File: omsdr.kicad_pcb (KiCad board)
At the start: 2 copper layers, 50 x 50 mm, 58 parts, among them J1 I/Q Out, J2 ANT, J3 ISP, J4 LO, J5 I/Q Out, J8 PWR, SW1 SW_SPST, SW2 SW_SPST, T1 CX2074NL, U1 LT6231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

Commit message: Adding year 2022 to copyright info
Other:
- board text added: "Based on work by T. Parks (c) 2017,18,19,22 CC-BY-SA"
- board text removed: "Based on work by T. Parks (c) 2017,18,19 CC-BY-SA"
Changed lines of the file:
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@@
   (gr_line (start 147.5 100) (end 102.5 100) (layer "Edge.Cuts") (width 0.15))
   (gr_arc (start 102.5 100) (mid 100.732233 99.267767) (end 100 97.5) (layer "Edge.Cuts") (width 0.15))
-  (gr_text "Based on work by T. Parks\n(c) 2017,18,19 CC-BY-SA" (at 148 89.25) (layer "B.SilkS")
+  (gr_text "Based on work by T. Parks\n(c) 2017,18,19,22 CC-BY-SA" (at 148 89.25) (layer "B.SilkS")
     (effects (font (size 0.75 0.75) (thickness 0.15)) (justify left mirror))
   )

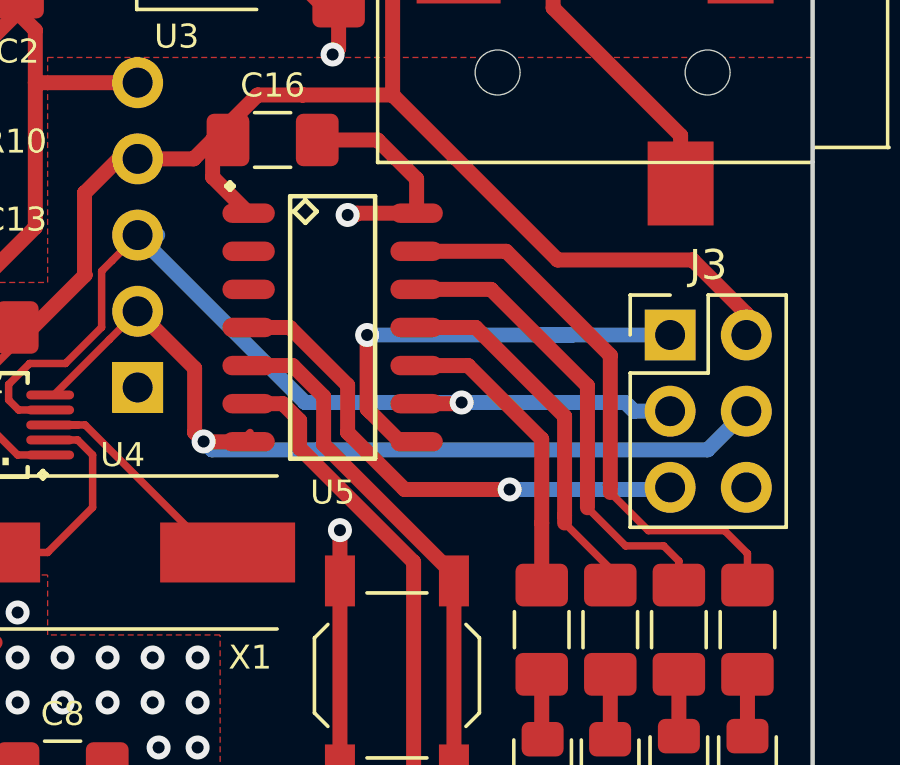
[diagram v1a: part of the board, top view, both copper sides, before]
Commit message: Using attiny24 from the KiCad library (sch & pcb)
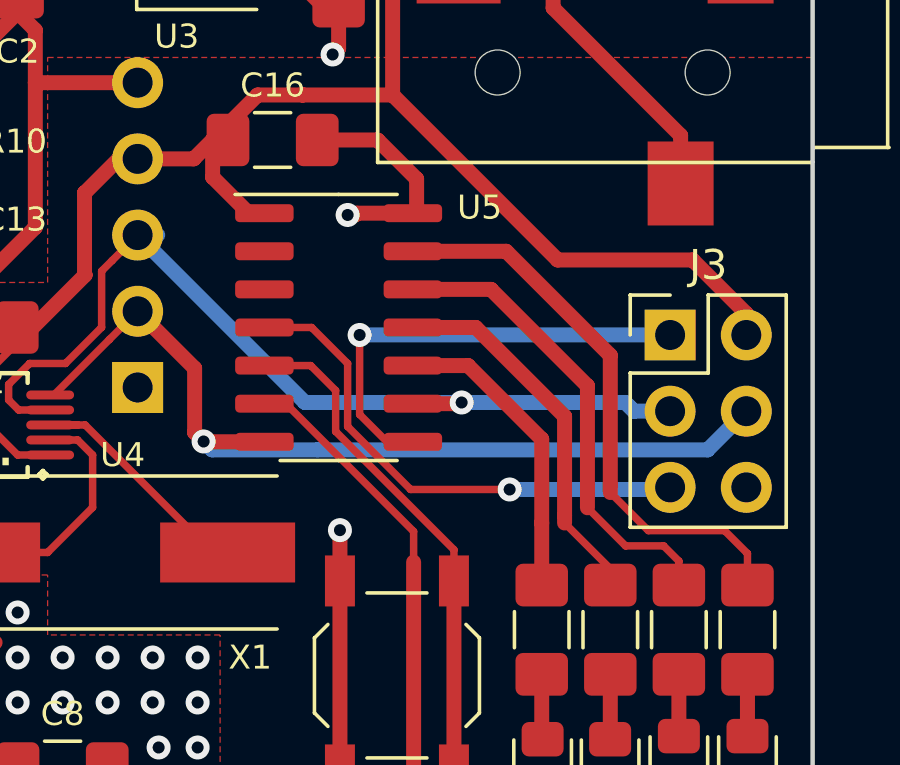
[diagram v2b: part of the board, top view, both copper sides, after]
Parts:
- U5: value ATTINY24-20SSU -> ATtiny24-20SS; footprint IPC7351-Most:SOIC127P600X175-14 -> Package_SO:SOIC-14_3.9x8.7mm_P1.27mm
- moved U5 0.20 mm to (134.2, 74.0)
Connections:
- net /MOSI renamed /SDA
- net /SCK renamed /SCL
- U2 pad 10: Net-(U2-Pad10) -> unconnected-(U2-Pad10)
- U2 pad 13: Net-(U2-Pad13) -> unconnected-(U2-Pad13)
- U2 pad 4: Net-(U2-Pad4) -> unconnected-(U2-Pad4)
- U2 pad 5: Net-(U2-Pad5) -> unconnected-(U2-Pad5)
- U4 pad 6: Net-(U4-Pad6) -> unconnected-(U4-Pad6)
- U5 pad 2: Net-(U5-Pad2) -> unconnected-(U5-Pad2)
- U5 pad 3: Net-(U5-Pad3) -> unconnected-(U5-Pad3)
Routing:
- net /SDA: track 30.3 -> 29.6 mm
- net /BUTTON2: track 24.9 -> 25.6 mm

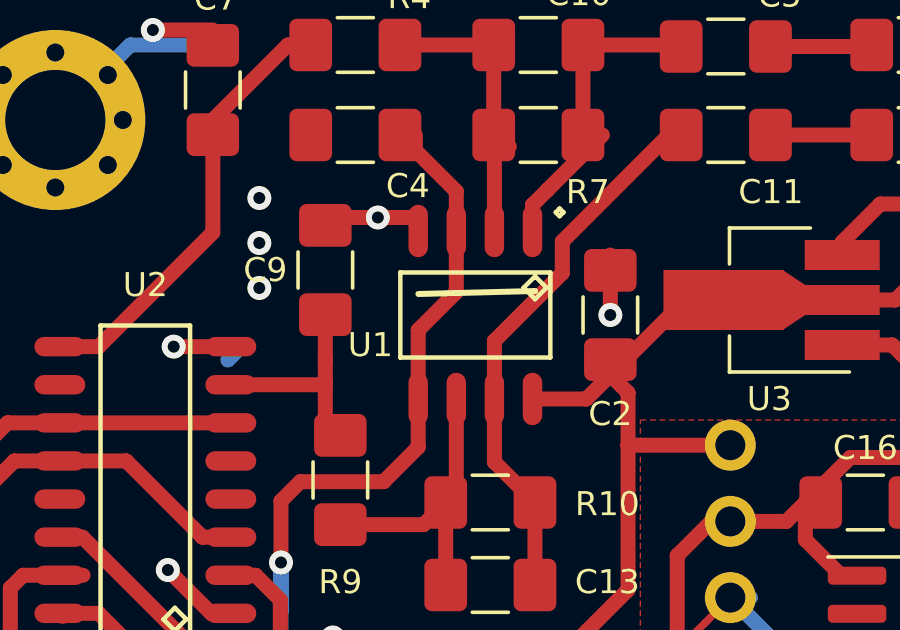
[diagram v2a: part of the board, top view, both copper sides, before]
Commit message: Using LC6231 from the KiCad library (sch & pcb)
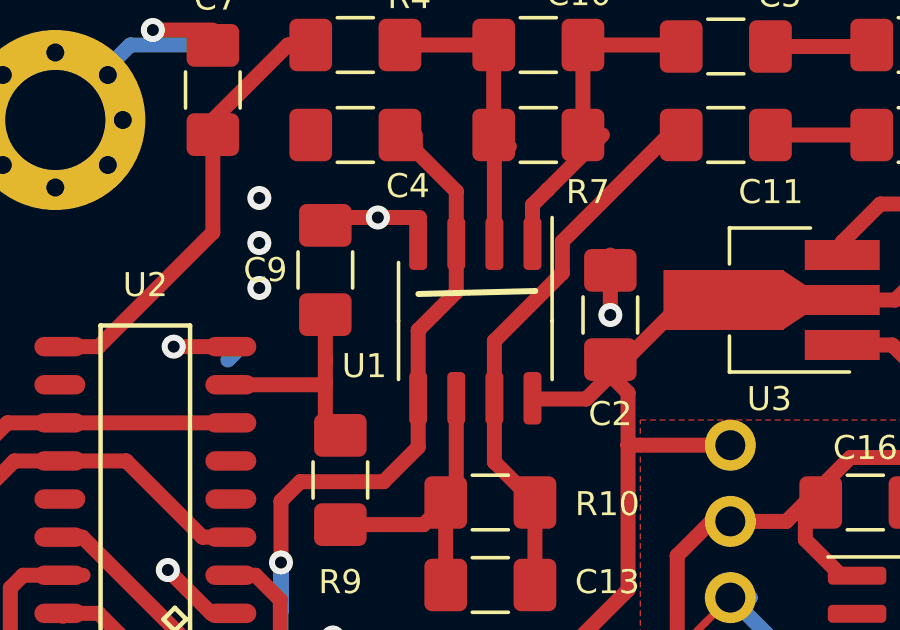
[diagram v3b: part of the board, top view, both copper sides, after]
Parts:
- U1: footprint IPC7351-Most:SOIC127P600X175-8 -> Package_SO:SO-8_3.9x4.9mm_P1.27mm
- moved U1 0.20 mm to (119.0, 61.7)
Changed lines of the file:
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@@
-    )
-  )
-  (footprint "IPC7351-Most:SOIC127P600X175-8" (layer "F.Cu")
-    (at 119 61.5 -90)
-    (descr "SOIC,1.27mm pitch;8 pin,4.00mm W X 5.00mm L X 1.75mm H Body")
-    (property "Sheetfile" "omsdr.kicad_sch")
-    (property "Sheetname" "")
-    (attr smd)
-    (fp_text reference "U1" (at 1 3.5) (layer "F.SilkS")
-      (effects (font (size 0.8 0.8) (thickness 0.15)))
-    )
-    (fp_text value "LT6231" (at 0 0 -90) (layer "F.Fab")
-      (effects (font (size 0.5 0.5) (thickness 0.1)))
-    )
-    (fp_line (start -0.909 -1.611) (end -1.29 -1.992) (layer "F.SilkS") (width 0.15))
-    (fp_line (start -3.548 -2.809) (end -3.421 -2.936) (layer "F.SilkS") (width 0.15))
-    (fp_line (start -3.421 -2.682) (end -3.548 -2.809) (layer "F.SilkS") (width 0.15))
-    (fp_line (start -1.417 -2.5) (end -1.417 2.5) (layer "F.SilkS") (width 0.15))
-    (fp_line (start -0.528 -1.992) (end -0.909 -1.611) (layer "F.SilkS") (width 0.15))
-    (fp_line (start -3.294 -2.809) (end -3.421 -2.682) (layer "F.SilkS") (width 0.15))
-    (fp_line (start -0.909 -2.373) (end -0.528 -1.992) (layer "F.SilkS") (width 0.15))
-    (fp_line (start 1.417 2.5) (end 1.417 -2.5) (layer "F.SilkS") (width 0.15))
-    (fp_line (start 1.417 -2.5) (end -1.417 -2.5) (layer "F.SilkS") (width 0.15))
-    (fp_line (start -1.417 2.5) (end 1.417 2.5) (layer "F.SilkS") (width 0.15))
-    (fp_line (start -3.421 -2.936) (end -3.294 -2.809) (layer "F.SilkS") (width 0.15))
-    (fp_line (start -1.29 -1.992) (end -0.909 -2.373) (layer "F.SilkS") (width 0.15))
-    (fp_line (start 4.175 3) (end -4.175 3) (layer "F.CrtYd") (width 0.05))
-    (fp_line (start -4.175 -3.436) (end 4.175 -3.436) (layer "F.CrtYd") (width 0.05))
-    (fp_line (start -4.175 3) (end -4.175 -3.436) (layer "F.CrtYd") (width 0.05))
-    (fp_line (start 4.175 -3.436) (end 4.175 3) (layer "F.CrtYd") (width 0.05))
-    (pad "1" smd oval locked (at -2.8 -1.905 270) (size 1.75 0.65) (layers "F.Cu" "F.Paste" "F.Mask")
-      (net 15 "Net-(C10-Pad2)") (pintype "output"))
-    (pad "2" smd oval locked (at -2.8 -0.635 270) (size 1.75 0.65) (layers "F.Cu" "F.Paste" "F.Mask")
-      (net 14 "Net-(C10-Pad1)") (pinfunction "-") (pintype "input"))
-    (pad "3" smd oval locked (at -2.8 0.635 270) (size 1.75 0.65) (layers "F.Cu" "F.Paste" "F.Mask")
-      (net 5 "/Vhalf") (pinfunction "+") (pintype "input"))
-    (pad "4" smd oval locked (at -2.8 1.905 270) (size 1.75 0.65) (layers "F.Cu" "F.Paste" "F.Mask")
-      (net 2 "GND") (pinfunction "V-") (pintype "power_in"))
-    (pad "5" smd oval locked (at 2.8 1.905 270) (size 1.75 0.65) (layers "F.Cu" "F.Paste" "F.Mask")
-      (net 5 "/Vhalf") (pinfunction "+") (pintype "input"))
-    (pad "6" smd oval locked (at 2.8 0.635 270) (size 1.75 0.65) (layers "F.Cu" "F.Paste" "F.Mask")
-      (net 10 "Net-(C13-Pad1)") (pinfunction "-") (pintype "input"))
-    (pad "7" smd oval locked (at 2.8 -0.635 270) (size 1.75 0.65) (layers "F.Cu" "F.Paste" "F.Mask")
-      (net 9 "Net-(C11-Pad1)") (pintype "output"))
-    (pad "8" smd oval locked (at 2.8 -1.905 270) (size 1.75 0.65) (layers "F.Cu" "F.Paste" "F.Mask")
-      (net 6 "+5V") (pinfunction "V+") (pintype "power_in"))
-    (model "smd_dil/so-8.wrl"
-      (offset (xyz 0 0 0))
-      (scale (xyz 1 1 1))
-      (rotate (xyz 0 0 90))
     )
   )
@@
       (offset (xyz 0 0 0))
       (scale (xyz 1 1 1))
+      (rotate (xyz 0 0 0))
+    )
+  )
+  (footprint "Package_SO:SO-8_3.9x4.9mm_P1.27mm" (layer "F.Cu")
+    (at 119 61.7 -90)
+    (descr "SO, 8 Pin (https://www.nxp.com/docs/en/data-sheet/PCF8523.pdf), generated with kicad-footprint-generator ipc_gullwing_generator.py")
+    (tags "SO SO")
+    (property "Sheetfile" "omsdr.kicad_sch")
+    (property "Sheetname" "")
+    (attr smd)
+    (fp_text reference "U1" (at 1.5 3.7 180) (layer "F.SilkS")
+      (effects (font (size 0.8 0.8) (thickness 0.15)))
+    )
+    (fp_text value "LT6231" (at 0 3.4 90) (layer "F.Fab")
+      (effects (font (size 1 1) (thickness 0.15)))
+    )
+    (fp_text user "${REFERENCE}" (at 0 0 90) (layer "F.Fab")
+      (effects (font (size 0.98 0.98) (thickness 0.15)))
+    )
+    (fp_line (start 0 2.56) (end -1.95 2.56) (layer "F.SilkS") (width 0.12))
+    (fp_line (start 0 -2.56) (end 1.95 -2.56) (layer "F.SilkS") (width 0.12))
+    (fp_line (start 0 -2.56) (end -3.45 -2.56) (layer "F.SilkS") (width 0.12))
+    (fp_line (start 0 2.56) (end 1.95 2.56) (layer "F.SilkS") (width 0.12))
+    (fp_line (start 3.7 2.7) (end 3.7 -2.7) (layer "F.CrtYd") (width 0.05))
+    (fp_line (start -3.7 -2.7) (end -3.7 2.7) (layer "F.CrtYd") (width 0.05))
+    (fp_line (start 3.7 -2.7) (end -3.7 -2.7) (layer "F.CrtYd") (width 0.05))
+    (fp_line (start -3.7 2.7) (end 3.7 2.7) (layer "F.CrtYd") (width 0.05))
+    (fp_line (start -1.95 2.45) (end -1.95 -1.475) (layer "F.Fab") (width 0.1))
+    (fp_line (start -0.975 -2.45) (end 1.95 -2.45) (layer "F.Fab") (width 0.1))
+    (fp_line (start 1.95 -2.45) (end 1.95 2.45) (layer "F.Fab") (width 0.1))
+    (fp_line (start 1.95 2.45) (end -1.95 2.45) (layer "F.Fab") (width 0.1))
+    (fp_line (start -1.95 -1.475) (end -0.975 -2.45) (layer "F.Fab") (width 0.1))
+    (pad "1" smd roundrect locked (at -2.575 -1.905 270) (size 1.75 0.6) (layers "F.Cu" "F.Paste" "F.Mask") (roundrect_rratio 0.25)
+      (net 15 "Net-(C10-Pad2)") (pintype "output"))
+    (pad "2" smd roundrect locked (at -2.575 -0.635 270) (size 1.75 0.6) (layers "F.Cu" "F.Paste" "F.Mask") (roundrect_rratio 0.25)
+      (net 14 "Net-(C10-Pad1)") (pinfunction "-") (pintype "input"))
+    (pad "3" smd roundrect locked (at -2.575 0.635 270) (size 1.75 0.6) (layers "F.Cu" "F.Paste" "F.Mask") (roundrect_rratio 0.25)
+      (net 5 "/Vhalf") (pinfunction "+") (pintype "input"))
+    (pad "4" smd roundrect locked (at -2.575 1.905 270) (size 1.75 0.6) (layers "F.Cu" "F.Paste" "F.Mask") (roundrect_rratio 0.25)
+      (net 2 "GND") (pinfunction "V-") (pintype "power_in"))
+    (pad "5" smd roundrect locked (at 2.575 1.905 270) (size 1.75 0.6) (layers "F.Cu" "F.Paste" "F.Mask") (roundrect_rratio 0.25)
+      (net 5 "/Vhalf") (pinfunction "+") (pintype "input"))
+    (pad "6" smd roundrect locked (at 2.575 0.635 270) (size 1.75 0.6) (layers "F.Cu" "F.Paste" "F.Mask") (roundrect_rratio 0.25)
+      (net 10 "Net-(C13-Pad1)") (pinfunction "-") (pintype "input"))
+    (pad "7" smd roundrect locked (at 2.575 -0.635 270) (size 1.75 0.6) (layers "F.Cu" "F.Paste" "F.Mask") (roundrect_rratio 0.25)
+      (net 9 "Net-(C11-Pad1)") (pintype "output"))
+    (pad "8" smd roundrect locked (at 2.575 -1.905 270) (size 1.75 0.6) (layers "F.Cu" "F.Paste" "F.Mask") (roundrect_rratio 0.25)
+      (net 6 "+5V") (pinfunction "V+") (pintype "power_in"))
+    (model "${KICAD6_3DMODEL_DIR}/Package_SO.3dshapes/SO-8_3.9x4.9mm_P1.27mm.wrl"
+      (offset (xyz 0 0 0))
+      (scale (xyz 1 1 1))

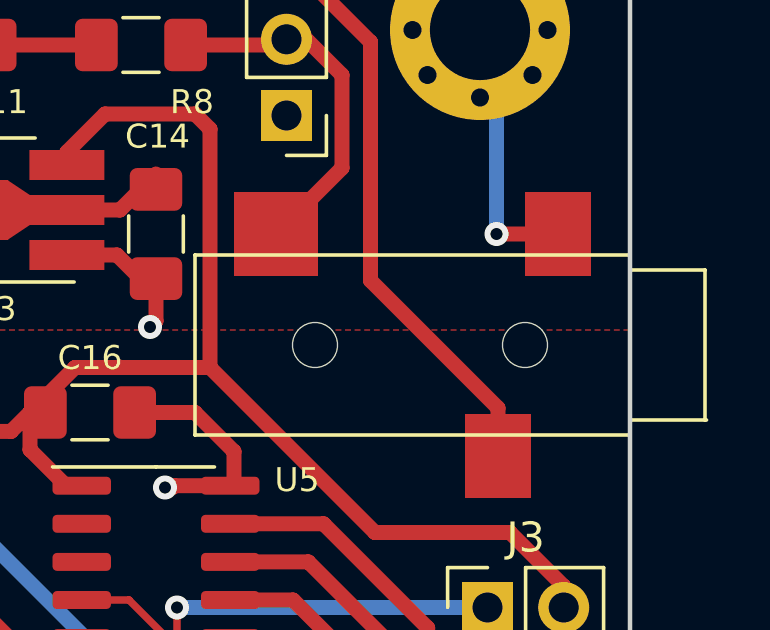
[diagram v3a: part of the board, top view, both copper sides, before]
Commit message: Using headphone connector from the KiCad library (sch & pcb)
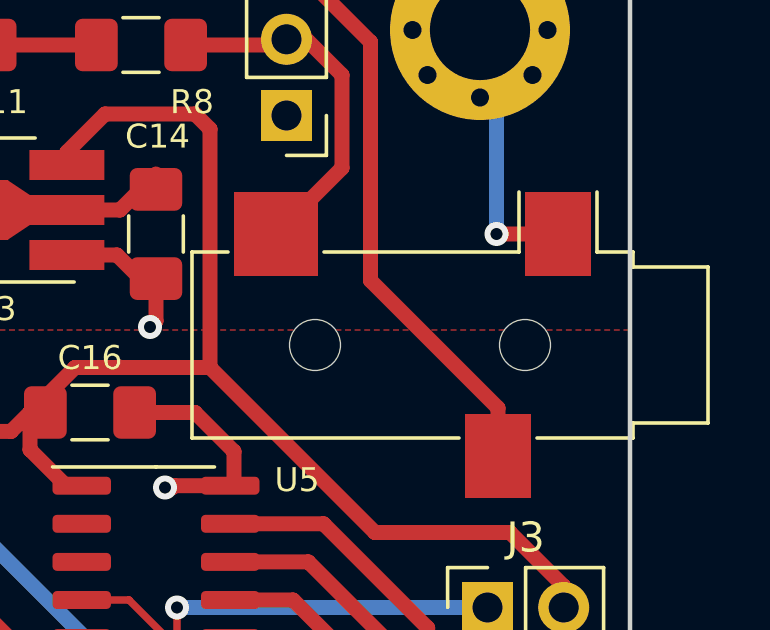
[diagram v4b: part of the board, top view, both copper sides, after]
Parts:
- J1: footprint conn-cui:CONN-SJ-3523-SMT -> Connector_Audio:Jack_3.5mm_CUI_SJ-3523-SMT_Horizontal
- moved J1 6.00 mm to (144.0, 65.5)
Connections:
- J5 pad 2: Net-(J1-Pad1) -> Net-(J5-Pad2)
- J5 pad 3: Net-(J1-Pad2) -> Net-(J5-Pad3)
- R3 pad 1: Net-(J1-Pad2) -> Net-(J5-Pad3)
- R8 pad 1: Net-(J1-Pad1) -> Net-(J5-Pad2)
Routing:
- net Net-(J5-Pad3): track 0.00 -> 23.4 mm
- net Net-(J1-Pad2): track 23.4 -> 0.00 mm
- net Net-(J5-Pad2): track 0.00 -> 12.3 mm
- net Net-(J1-Pad1): track 12.3 -> 0.00 mm

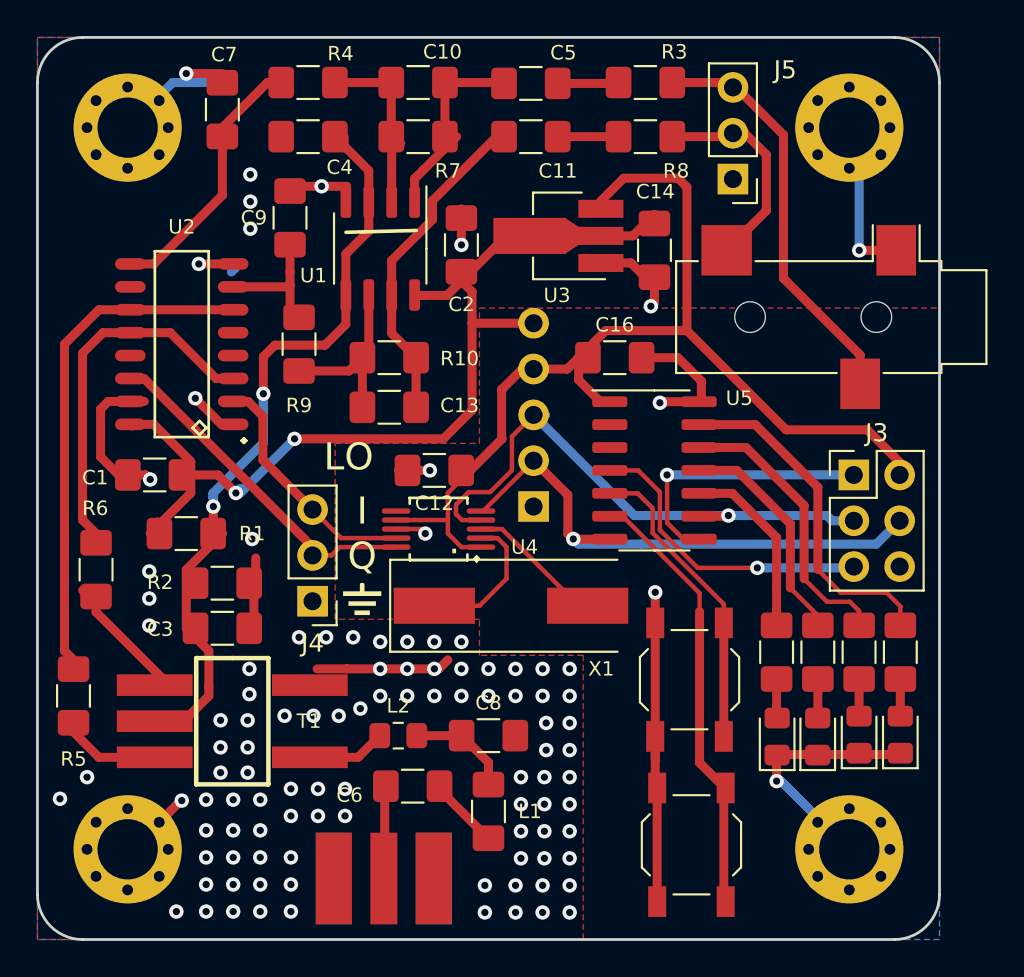
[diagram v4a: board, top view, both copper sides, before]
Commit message: Using Si5351 from the KiCad library (sch & pcb)
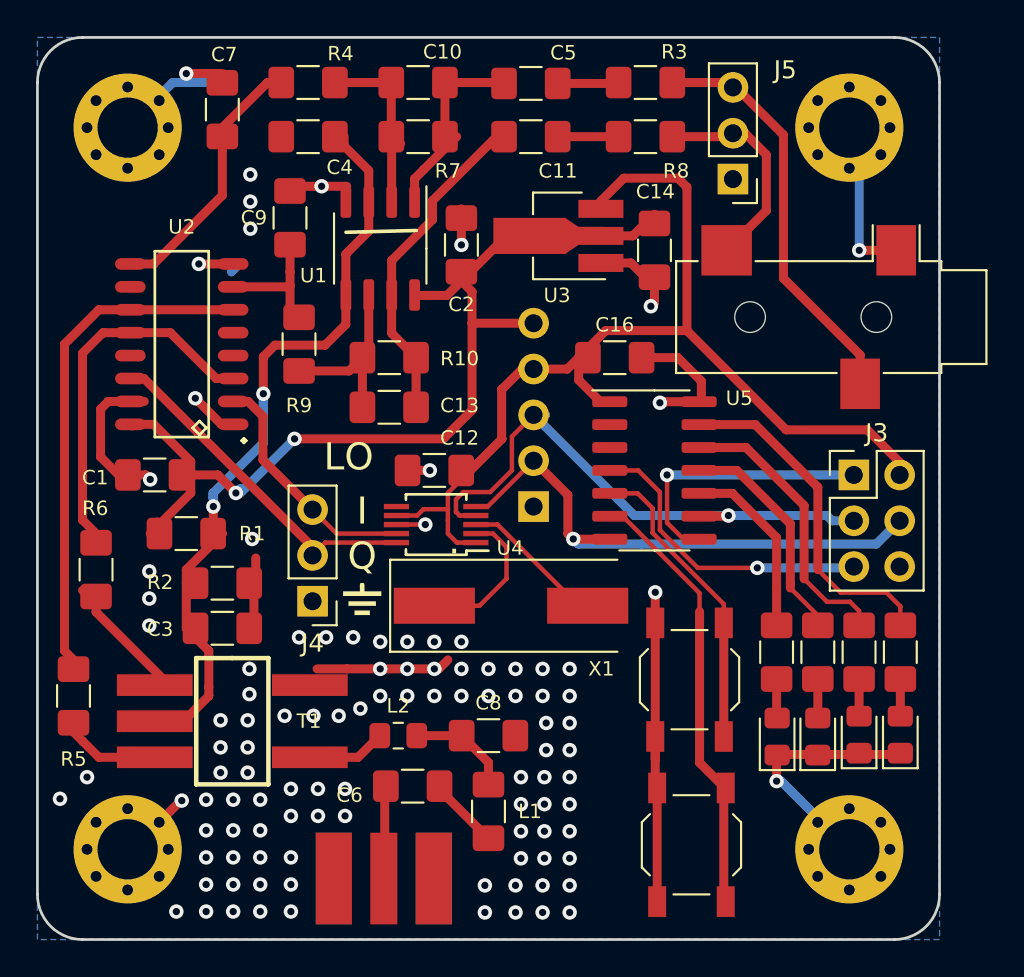
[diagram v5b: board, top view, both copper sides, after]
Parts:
- U4: value Si5351A -> Si5351A-B-GT; footprint IPC7351-Most:SOP50P490X110-10 -> Package_SO:MSOP-10_3x3mm_P0.5mm
- moved U4 0.28 mm to (122.1, 77.0)
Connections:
- net /SCL renamed /SCK
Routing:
- net GND: track 99.3 -> 98.7 mm
- net Net-(U4-Pad3): track 9.34 -> 8.81 mm
- removed copper zone on F.Cu, net GND
